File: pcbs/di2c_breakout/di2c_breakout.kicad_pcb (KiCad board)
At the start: 2 copper layers, 17.8 x 21 mm, 16 parts, among them P1 CONN_02X05, P2 CONN_01X04, P3 CONN_01X04, U1 PCA9615

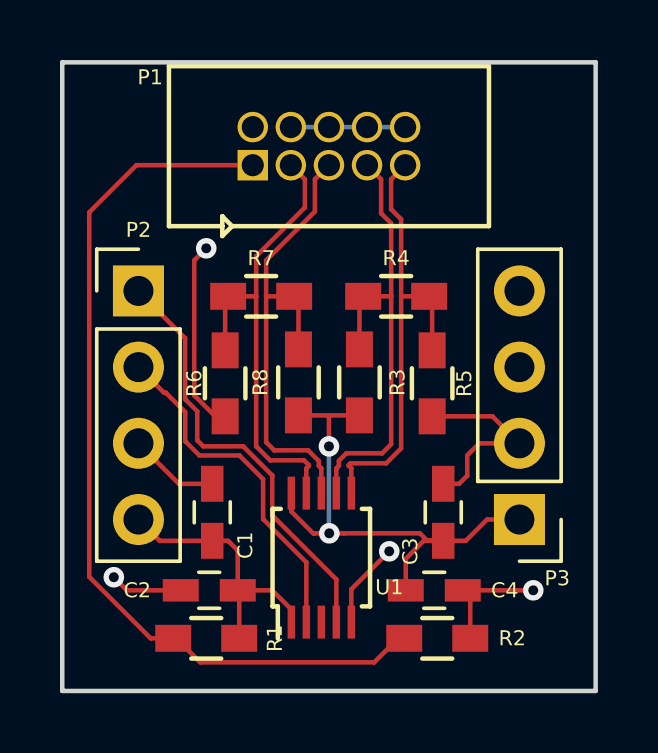
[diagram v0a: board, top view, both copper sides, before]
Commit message: added beginnings of a bno055 driver
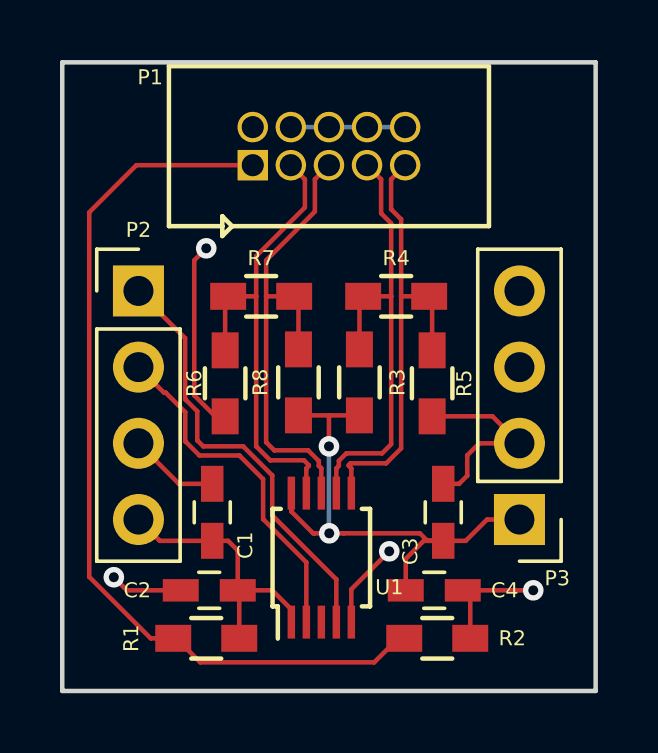
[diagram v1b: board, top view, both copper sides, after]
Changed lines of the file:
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@@
     (tags "resistor 0603")
     (attr smd)
-    (fp_text reference R1 (at 2.286 0 90) (layer F.SilkS)
+    (fp_text reference R1 (at -2.5 0 90) (layer F.SilkS)
       (effects (font (size 0.5 0.5) (thickness 0.1)))
     )
